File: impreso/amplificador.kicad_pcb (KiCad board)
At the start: 2 copper layers, 81 parts, among them Q1 2SC3281, Q10 MPSA42, Q11 2SC3281, Q12 2SA1302, Q13 MPSA92, Q14 MPSA92, Q15 MJE340, Q16 MJE350, Q2 MJE340, Q20 2SA1302, Q3 MJE340, Q4 2SC3281, Q6 MJE350, Q7 2SA1302, Q8 MJE350, Q9 MPSA42, T3 TORNILLO, T4 TORNILLO, T5 TORNILLO, T6 TORNILLO, T7 TORNILLO, T8 TORNILLO, U1 MMPQ2222A, U2 MMPQ2907A, U3 LM7809CT, U4 LM7909CT

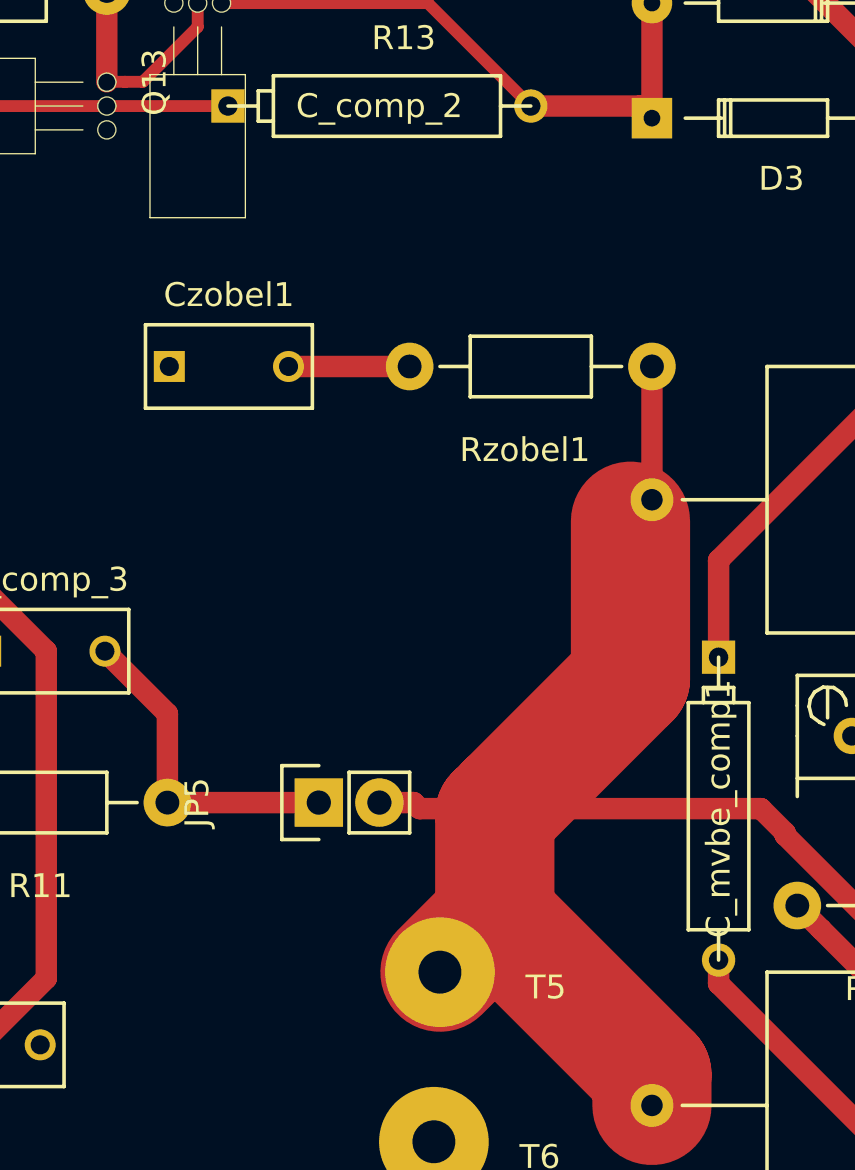
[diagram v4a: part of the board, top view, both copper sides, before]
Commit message: Agregué el separador de capacitancia de carga al esquemático y al PCB.
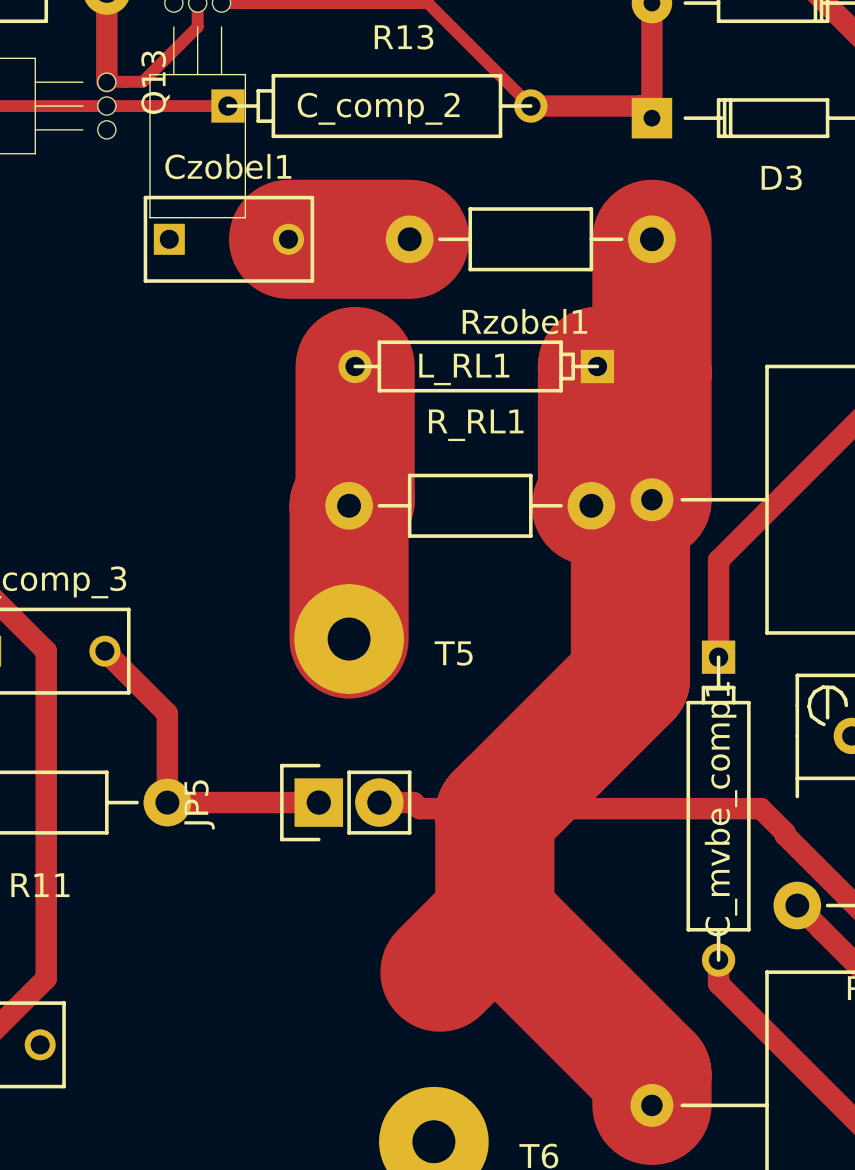
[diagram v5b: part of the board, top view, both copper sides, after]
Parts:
- added L_RL1: 5u, Discret:CP4, F.Cu at (89.2, 83.3)
- added R_RL1: 10R, Resistors_ThroughHole:Resistor_Horizontal_RM10mm, F.Cu at (88.9, 89.2)
- moved T5 14.5 mm to (83.8, 97.3)
- moved Czobel1 5.33 mm to (76.3, 78.0)
- moved Rzobel1 5.33 mm to (91.4, 78.0)
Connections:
- T5 pad 1: Realim -> Salida
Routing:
- net Realim: track 86.3 -> 107.9 mm
- net Salida: track 0.00 -> 11.5 mm
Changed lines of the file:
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@@
 (kicad_pcb (version 4) (host pcbnew 0.201512080931+6353~38~ubuntu14.04.1-stable)
   (general
-    (links 147)
-    (no_connects 39)
+    (links 150)
+    (no_connects 35)
     (area 0 0 0 0)
     (thickness 1.6)
     (drawings 0)
-    (tracks 374)
+    (tracks 384)
     (zones 0)
-    (modules 81)
-    (nets 57)
+    (modules 83)
+    (nets 58)
   )
   (page A4)
@@
   (net 55 "Net-(R_curr2-Pad2)")
   (net 56 "Net-(Czobel1-Pad2)")
+  (net 57 Salida)
   (net_class Default "This is the default net class."
     (clearance 0.2)
@@
     (add_net "Net-(U2-Pad16)")
     (add_net Realim)
+    (add_net Salida)
   )
   (module TO_SOT_Packages_THT:SOT126_SOT32_Housing_Vertical (layer F.Cu)
@@
   )
   (module bibliotecas:TORNILLO (layer F.Cu)
-    (at 87.63 111.252)
+    (at 83.82 97.282)
     (fp_text reference T5 (at 4.445 -1.905) (layer F.SilkS)
       (effects (font (size 1 1) (thickness 0.15)))
@@
     )
     (pad 1 thru_hole circle (at 0 -2.54) (size 4.6 4.6) (drill 1.8) (layers *.Mask B.Cu F.SilkS)
-      (net 30 Realim))
+      (net 57 Salida))
   )
   (module bibliotecas:TORNILLO (layer F.Cu)
@@
   )
   (module Capacitors_ThroughHole:C_Rect_L7_W3.5_P5 (layer F.Cu)
-    (at 76.28 83.312)
+    (at 76.28 77.978)
     (descr "Film Capacitor Length 7mm x Width 3.5mm, Pitch 5mm")
     (tags Capacitor)
@@
   )
   (module Resistors_ThroughHole:Resistor_Horizontal_RM10mm (layer F.Cu)
-    (at 91.44 83.312 180)
+    (at 91.44 77.978 180)
     (descr "Resistor, Axial,  RM 10mm, 1/3W,")
     (tags "Resistor, Axial, RM 10mm, 1/3W,")
@@
       (net 6 -50))
     (model Resistors_ThroughHole.3dshapes/Resistor_Horizontal_RM10mm.wrl
+      (at (xyz 0 0 0))
+      (scale (xyz 0.4 0.4 0.4))
+      (rotate (xyz 0 0 0))
+    )
+  )
+  (module Resistors_ThroughHole:Resistor_Horizontal_RM10mm (layer F.Cu)
+    (at 88.9 89.154)
+    (descr "Resistor, Axial,  RM 10mm, 1/3W,")
+    (tags "Resistor, Axial, RM 10mm, 1/3W,")
+    (fp_text reference R_RL1 (at 0.24892 -3.50012) (layer F.SilkS)
+      (effects (font (size 1 1) (thickness 0.15)))
+    )
+    (fp_text value 10R (at 3.81 3.81) (layer F.Fab)
+      (effects (font (size 1 1) (thickness 0.15)))
+    )
+    (fp_line (start -2.54 -1.27) (end 2.54 -1.27) (layer F.SilkS) (width 0.15))
+    (fp_line (start 2.54 -1.27) (end 2.54 1.27) (layer F.SilkS) (width 0.15))
+    (fp_line (start 2.54 1.27) (end -2.54 1.27) (layer F.SilkS) (width 0.15))
+    (fp_line (start -2.54 1.27) (end -2.54 -1.27) (layer F.SilkS) (width 0.15))
+    (fp_line (start -2.54 0) (end -3.81 0) (layer F.SilkS) (width 0.15))
+    (fp_line (start 2.54 0) (end 3.81 0) (layer F.SilkS) (width 0.15))
+    (pad 1 thru_hole circle (at -5.08 0) (size 1.99898 1.99898) (drill 1.00076) (layers *.Cu *.SilkS *.Mask)
+      (net 57 Salida))
+    (pad 2 thru_hole circle (at 5.08 0) (size 1.99898 1.99898) (drill 1.00076) (layers *.Cu *.SilkS *.Mask)
+      (net 30 Realim))
+    (model Resistors_ThroughHole.3dshapes/Resistor_Horizontal_RM10mm.wrl
+      (at (xyz 0 0 0))
+      (scale (xyz 0.4 0.4 0.4))
+      (rotate (xyz 0 0 0))
+    )
+  )
+  (module Discret:CP4 (layer F.Cu)
+    (at 89.154 83.312 180)
+    (descr "Condensateur polarise")
+    (tags CP)
+    (fp_text reference L_RL1 (at 0.508 0 180) (layer F.SilkS)
+      (effects (font (size 1 1) (thickness 0.15)))
+    )
+    (fp_text value 5u (at 0.508 0 180) (layer F.Fab)
+      (effects (font (size 1 1) (thickness 0.15)))
+    )
+    (fp_line (start 5.08 0) (end 4.064 0) (layer F.SilkS) (width 0.15))
+    (fp_line (start 4.064 0) (end 4.064 1.016) (layer F.SilkS) (width 0.15))
+    (fp_line (start 4.064 1.016) (end -3.556 1.016) (layer F.SilkS) (width 0.15))
+    (fp_line (start -3.556 1.016) (end -3.556 -1.016) (layer F.SilkS) (width 0.15))
+    (fp_line (start -3.556 -1.016) (end 4.064 -1.016) (layer F.SilkS) (width 0.15))
+    (fp_line (start 4.064 -1.016) (end 4.064 0) (layer F.SilkS) (width 0.15))
+    (fp_line (start -5.08 0) (end -4.064 0) (layer F.SilkS) (width 0.15))
+    (fp_line (start -3.556 0.508) (end -4.064 0.508) (layer F.SilkS) (width 0.15))
+    (fp_line (start -4.064 0.508) (end -4.064 -0.508) (layer F.SilkS) (width 0.15))
+    (fp_line (start -4.064 -0.508) (end -3.556 -0.508) (layer F.SilkS) (width 0.15))
+    (pad 1 thru_hole rect (at -5.08 0 180) (size 1.397 1.397) (drill 0.8128) (layers *.Cu *.Mask F.SilkS)
+      (net 30 Realim))
+    (pad 2 thru_hole circle (at 5.08 0 180) (size 1.397 1.397) (drill 0.8128) (layers *.Cu *.Mask F.SilkS)
+      (net 57 Salida))
+    (model Discret.3dshapes/CP4.wrl
       (at (xyz 0 0 0))
       (scale (xyz 0.4 0.4 0.4))
@@
   (segment (start 57.15 62.23) (end 64.77 62.23) (width 0.9) (layer F.Cu) (net 28))
   (segment (start 57.15 138.43) (end 66.04 138.43) (width 0.9) (layer F.Cu) (net 29))
+  (segment (start 94.234 83.312) (end 94.234 88.9) (width 5) (layer F.Cu) (net 30))
+  (segment (start 96.52 88.9) (end 96.52 83.566) (width 5) (layer F.Cu) (net 30))
+  (segment (start 96.52 83.566) (end 96.52 77.978) (width 5) (layer F.Cu) (net 30))
+  (segment (start 94.234 83.312) (end 96.266 83.312) (width 5) (layer F.Cu) (net 30))
+  (segment (start 96.266 83.312) (end 96.52 83.566) (width 5) (layer F.Cu) (net 30))
+  (segment (start 96.52 88.9) (end 94.234 88.9) (width 5) (layer F.Cu) (net 30))
+  (segment (start 94.234 88.9) (end 93.98 89.154) (width 5) (layer F.Cu) (net 30))
   (segment (start 96.52 83.312) (end 96.52 88.9) (width 0.9) (layer F.Cu) (net 30))
   (segment (start 96.52 114.3) (end 96.52 113.002002) (width 5) (layer F.Cu) (net 30))
@@
   (segment (start 52.650002 119.38) (end 53.34 118.690002) (width 0.9) (layer F.Cu) (net 53))
   (segment (start 46.99 114.3) (end 51.55 114.3) (width 0.9) (layer F.Cu) (net 55))
-  (segment (start 81.28 83.312) (end 86.36 83.312) (width 0.9) (layer F.Cu) (net 56))
+  (segment (start 86.36 77.978) (end 81.28 77.978) (width 5) (layer F.Cu) (net 56))
+  (segment (start 83.82 89.154) (end 83.82 94.742) (width 5) (layer F.Cu) (net 57))
+  (segment (start 84.074 83.312) (end 84.074 88.9) (width 5) (layer F.Cu) (net 57))
+  (segment (start 84.074 88.9) (end 83.82 89.154) (width 5) (layer F.Cu) (net 57))
   (zone (net 2) (net_name EntradaGND) (layer B.Cu) (hatch edge 0.508)
     (connect_pads (clearance 0.508))

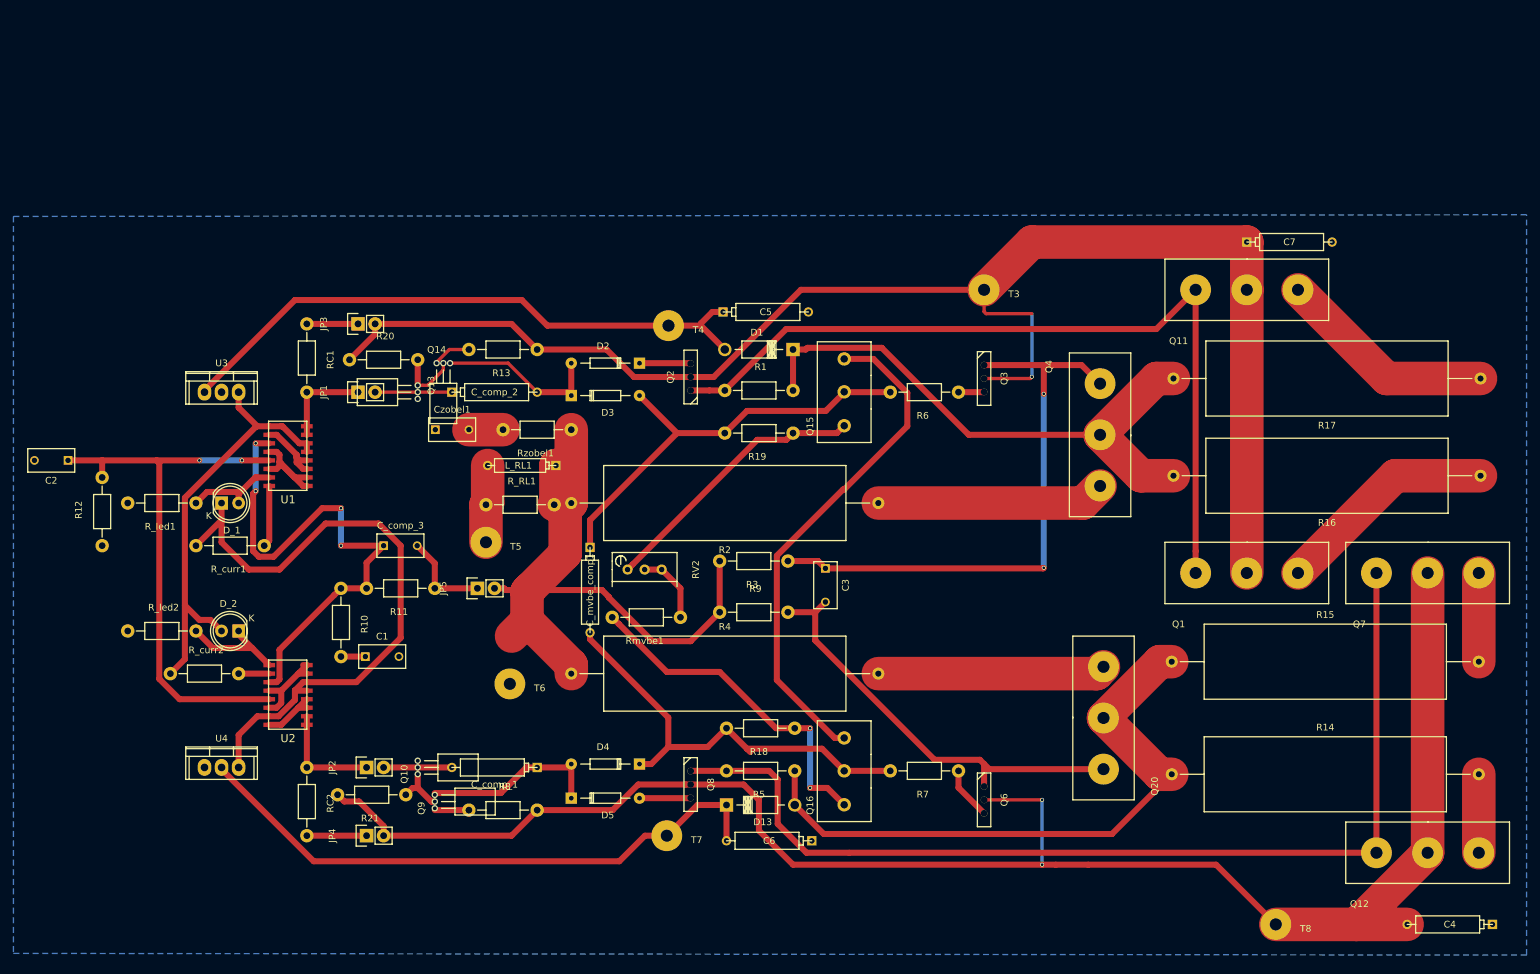
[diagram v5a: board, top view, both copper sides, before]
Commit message: Se hizo el ruteo con los nuevos componentes, y se corrigieron los valores de las protecciones, corrigiendo las disparidades.
Ya se mandó el circuito al LCI, para hacer.
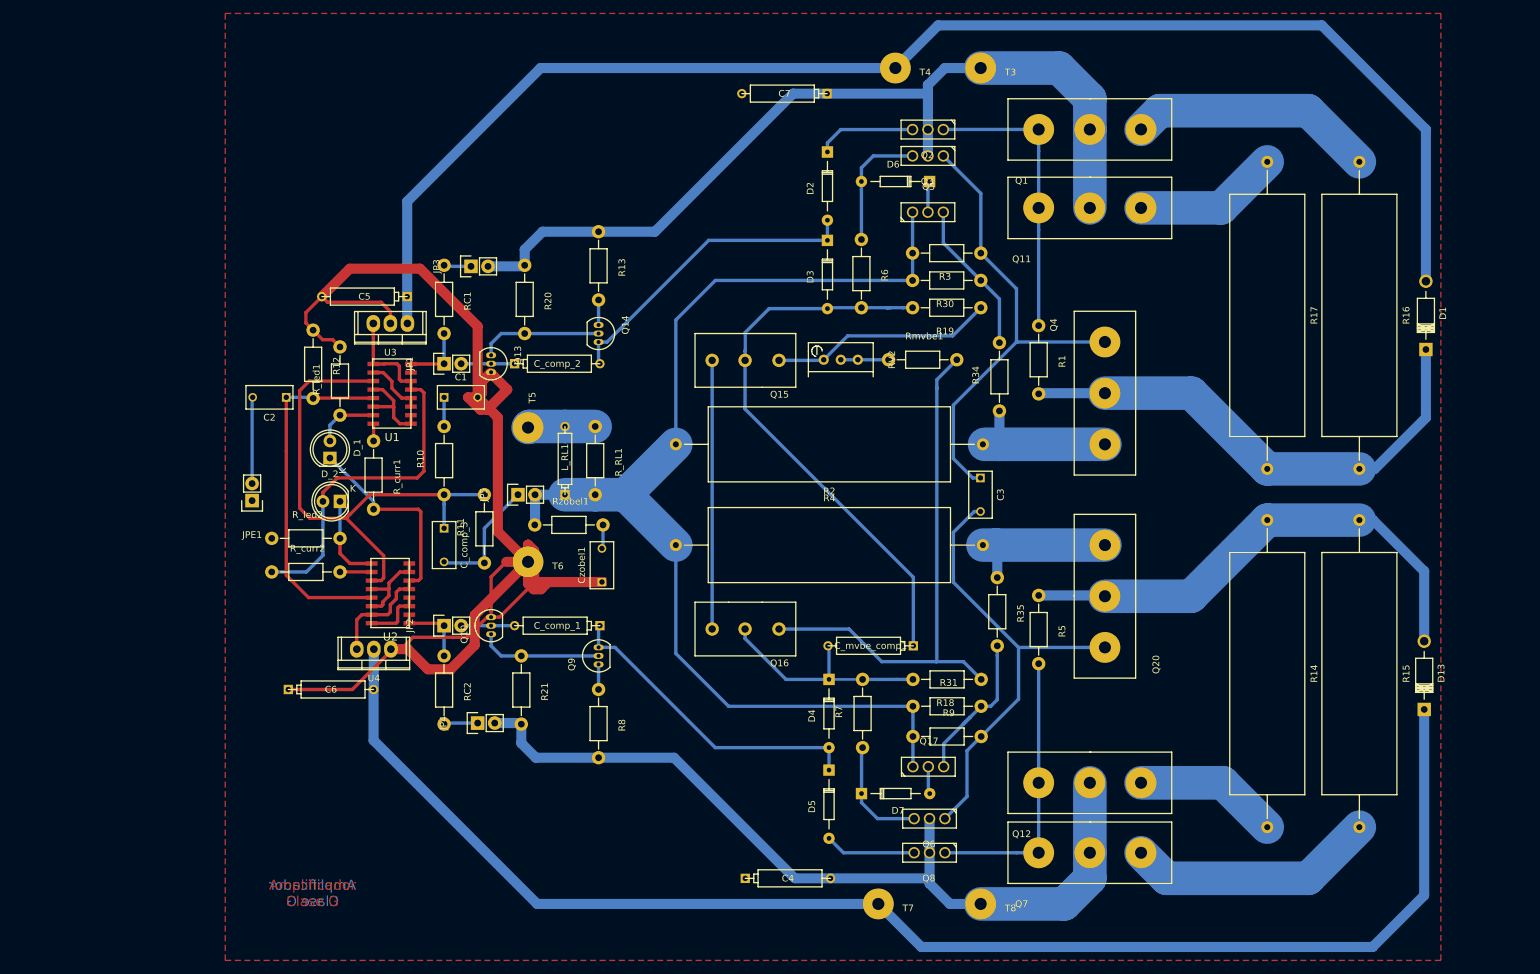
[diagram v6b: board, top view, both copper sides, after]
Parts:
- added D6: D1N4148, Diodes_ThroughHole:Diode_DO-35_SOD27_Horizontal_RM10, F.Cu at (149.9, 41.0)
- added D7: D1N4148, Diodes_ThroughHole:Diode_DO-35_SOD27_Horizontal_RM10, F.Cu at (139.7, 132.2)
- added JPE1: JUMPER, Pin_Headers:Pin_Header_Straight_1x02, F.Cu at (49.0, 88.5)
- added Q17: MJE350, TO_SOT_Packages_THT:SOT126_SOT32_Housing_Vertical, F.Cu at (149.7, 128.2)
- added Q5: MJE340, TO_SOT_Packages_THT:SOT126_SOT32_Housing_Vertical, F.Cu at (149.6, 45.6)
- added R30: 68R, Resistors_ThroughHole:Resistor_Horizontal_RM10mm, F.Cu at (157.5, 55.8)
- added R31: 51R, Resistors_ThroughHole:Resistor_Horizontal_RM10mm, F.Cu at (147.4, 119.2)
- added R34: 51R, Resistors_ThroughHole:Resistor_Horizontal_RM10mm, F.Cu at (160.3, 75.2)
- added R35: 51R, Resistors_ThroughHole:Resistor_Horizontal_RM10mm, F.Cu at (159.9, 100.0)
- Q10, Q13, Q14, Q9: footprint TO_SOT_Packages_THT:TO-92_Horizontal1_Inline_Narrow_Oval -> TO_SOT_Packages_THT:TO-92_Inline_Narrow_Oval
- moved D13 104.9 mm to (223.5, 119.6), turned to 90 degrees
- moved C4 98.8 mm to (128.8, 144.8), turned to 0 degrees
- moved D1 94.2 mm to (223.8, 66.0), turned to 90 degrees
- moved C7 78.4 mm to (128.3, 27.9), turned to 180 degrees
- moved Q1 70.1 mm to (173.7, 33.3)
- moved C6 69.0 mm to (60.7, 116.7), turned to 0 degrees
- moved Q7 65.3 mm to (173.7, 141.0)
- moved C5 59.8 mm to (65.7, 58.2), turned to 180 degrees
- moved R3 57.0 mm to (157.5, 51.7)
- moved Rmvbe1 52.6 mm to (143.8, 67.6), turned to 0 degrees
- moved Q12 51.4 mm to (173.7, 130.6)
- moved T4 51.1 mm to (144.8, 26.7)
- moved Q2 51.0 mm to (149.6, 33.3), turned to 180 degrees
- moved R5 49.0 mm to (166.1, 102.7), turned to 270 degrees
- moved D3 44.6 mm to (134.7, 49.8), turned to 270 degrees
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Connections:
- net EntradaGND renamed SalidaGND
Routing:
- net SalidaGND: track 0.00 -> 239.6 mm, vias 1 -> 0
- net -15: track 89.9 -> 224.5 mm
- net -50: track 263.5 -> 131.1 mm, vias 2 -> 0
- net +15: track 90.7 -> 209.7 mm
- net Net-(Q12-Pad1): track 152.7 -> 42.1 mm
- net Net-(Q1-Pad1): track 123.6 -> 43.4 mm
- net (no net): track 76.0 -> 0.00 mm
- net +50: track 224.7 -> 153.1 mm, vias 1 -> 0
- net Realim: track 107.9 -> 172.7 mm
- net Net-(D_1-Pad1): track 95.1 -> 45.9 mm
- net Net-(Q15-Pad1): track 0.00 -> 40.0 mm
- net Net-(C_mvbe_comp1-Pad2): track 64.7 -> 34.5 mm
- net Net-(C2-Pad1): track 82.8 -> 54.2 mm, vias 2 -> 0
- net Net-(Q16-Pad3): track 51.3 -> 79.7 mm, vias 2 -> 0
- net Net-(Q7-Pad3): track 13.2 -> 37.2 mm
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- added copper zone on F.Cu, net SalidaGND
- removed copper zone on B.Cu, net SalidaGND
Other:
- net class Default: clearance 0.2 -> 0.25; trace_width 0.9 -> 0.5; via_dia 0.6 -> 0.8
- net class Potencia added: clearance 0.25, trace_width 5, via_dia 0.8, via_drill 0.4
- rule trace_clearance: 0.2 -> 0.25
- board text added: "Amplificador Clase G"
